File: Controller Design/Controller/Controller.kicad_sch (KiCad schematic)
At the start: 48 parts, among them J1 USB_C_Receptacle_USB2.0, J2 JTAG, J3 UART, J4 FAN0, J5 FAN1, J6 FAN2, SW1 SW_MEC_5G, SW2 BOOT, SW3 RotaryEncoder_Switch, U1 ESP32-S3-WROOM-2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

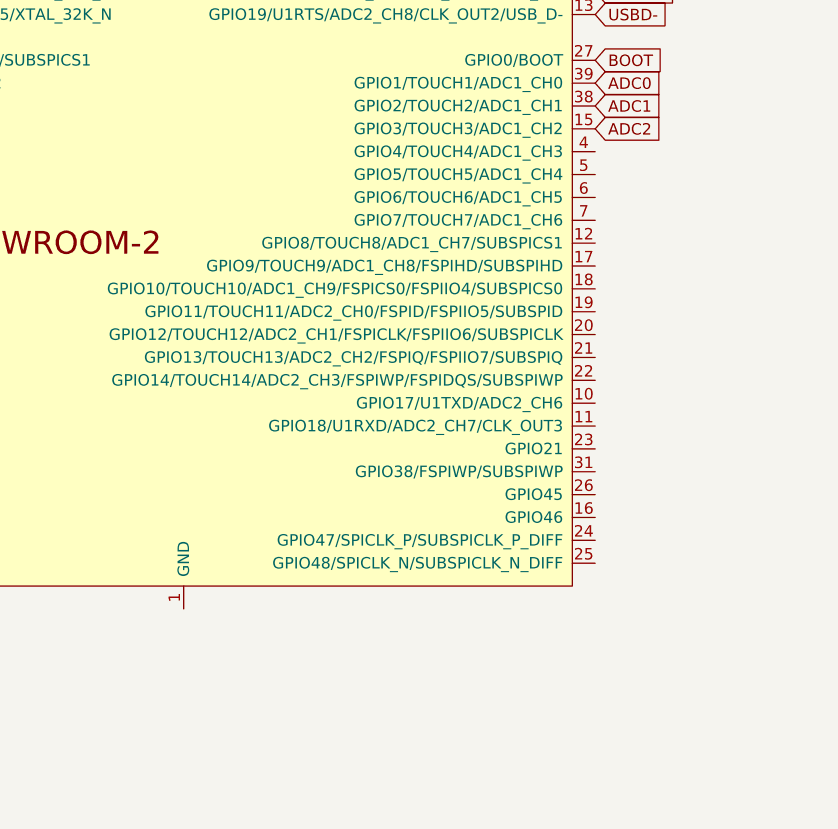
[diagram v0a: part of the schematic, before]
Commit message: devlog: concerns with power
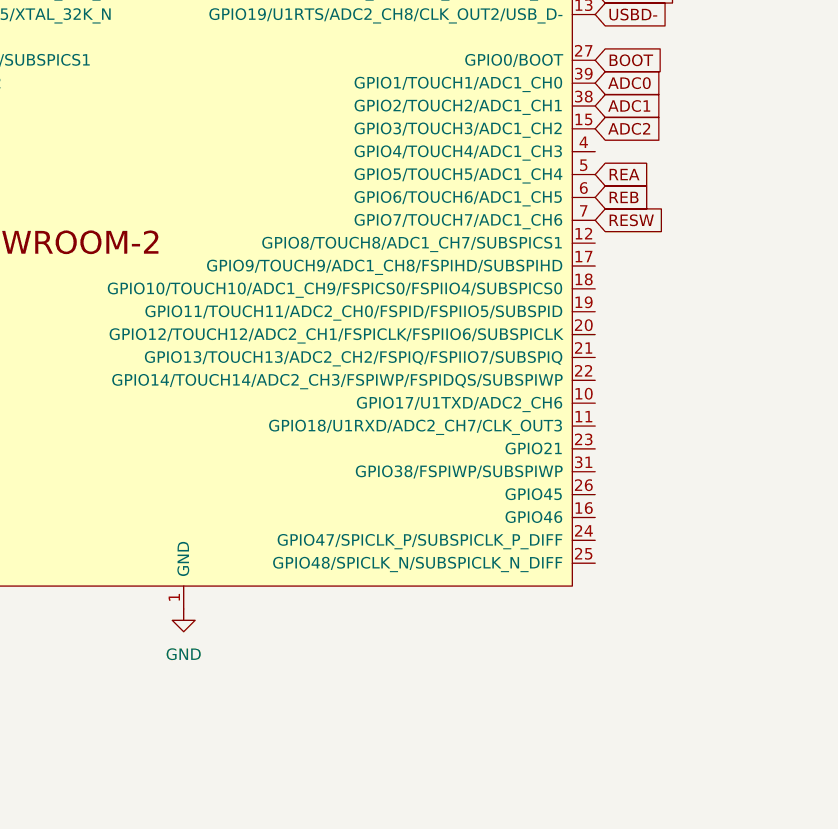
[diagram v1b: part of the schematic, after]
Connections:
- net GND: now also U1.1 (GND), U1.40 (GND), U1.41 (GND)
- net REA: now also U1.5 (GPIO5/TOUCH5/ADC1_CH4)
- net REB: now also U1.6 (GPIO6/TOUCH6/ADC1_CH5)
- net RESW: now also U1.7 (GPIO7/TOUCH7/ADC1_CH6)
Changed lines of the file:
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@@
+    )
+  )
+  (global_label "RESW" (shape input) (at 144.78 102.87 0) (fields_autoplaced)
+    (effects (font (size 1.27 1.27)) (justify left))
+    (property "Intersheetrefs" "${INTERSHEET_REFS}" (at 154.0357 102.87 0)
+      (effects (font (size 1.27 1.27)) (justify left) hide)
     )
   )
@@
     )
   )
+  (global_label "REB" (shape input) (at 144.78 100.33 0) (fields_autoplaced)
+    (effects (font (size 1.27 1.27)) (justify left))
+    (property "Intersheetrefs" "${INTERSHEET_REFS}" (at 151.3748 100.33 0)
+      (effects (font (size 1.27 1.27)) (justify left) hide)
+    )
+  )
   (global_label "TMS" (shape input) (at 229.87 114.3 180) (fields_autoplaced)
     (effects (font (size 1.27 1.27)) (justify right))
@@
     (effects (font (size 1.27 1.27)) (justify left))
     (property "Intersheetrefs" "${INTERSHEET_REFS}" (at 154.3382 80.01 0)
+      (effects (font (size 1.27 1.27)) (justify left) hide)
+    )
+  )
+  (global_label "REA" (shape input) (at 144.78 97.79 0) (fields_autoplaced)
+    (effects (font (size 1.27 1.27)) (justify left))
+    (property "Intersheetrefs" "${INTERSHEET_REFS}" (at 151.1934 97.79 0)
       (effects (font (size 1.27 1.27)) (justify left) hide)
     )
@@
         )
       )
+    )
+  )
+  (symbol (lib_id "power:GND") (at 99.06 146.05 0) (unit 1)
+    (in_bom yes) (on_board yes) (dnp no) (fields_autoplaced)
+    (property "Reference" "#PWR038" (at 99.06 152.4 0)
+      (effects (font (size 1.27 1.27)) hide)
+    )
+    (property "Value" "GND" (at 99.06 151.13 0)
+      (effects (font (size 1.27 1.27)))
+    )
+    (property "Footprint" "" (at 99.06 146.05 0)
+      (effects (font (size 1.27 1.27)) hide)
+    )
+    (property "Datasheet" "" (at 99.06 146.05 0)
+      (effects (font (size 1.27 1.27)) hide)
+    )
+    (pin "1")
+    (instances
+      (project "Controller"
+        (path "/3ce940e4-bb4c-4a70-948a-7cd3ff5c738d"
+          (reference "#PWR038") (unit 1)
+        )
+      )

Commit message: cleaned up schematic
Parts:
- added D1, D2: D_Schottky, Diode_SMD:D_0805_2012Metric_Pad1.15x1.40mm_HandSolder, symbol Device:D_Schottky
- added J7: Molex Socket, symbol Connector:Conn_01x04_Socket
- added U5: AP2112K-3.3, Package_TO_SOT_SMD:SOT-23-5, symbol Regulator_Linear:AP2112K-3.3
- C1, C10, C11, C2, C3, C4, C5, C6, C7, C8, C9: footprint (none) -> Capacitor_SMD:C_0805_2012Metric_Pad1.18x1.45mm_HandSolder
- R1, R11, R12, R15, R16, R18, R2, R3, R4, R5, R6, R7, R8, R9, TH1: footprint (none) -> Resistor_SMD:R_0805_2012Metric_Pad1.20x1.40mm_HandSolder
- R10, R13, R14, R17: value 60k -> 50k; footprint (none) -> Resistor_SMD:R_0805_2012Metric_Pad1.20x1.40mm_HandSolder
- R19, R20, R21: value R -> 1k; footprint (none) -> Resistor_SMD:R_0805_2012Metric_Pad1.20x1.40mm_HandSolder
- SW1: value SW_MEC_5G -> RESET
- U2, U3, U4: value Opamp_Dual -> LM2904DR; footprint (none) -> Package_SO:SOIC-8_3.9x4.9mm_P1.27mm
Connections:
- net +3.3V: now also U5.5 (VOUT)
- net GND: now also J7.2 (Pin_2), J7.3 (Pin_3), U5.2 (GND)
- net 5vUsb: now reaches J1.A4 (VBUS), J1.A9 (VBUS), J1.B4 (VBUS), J1.B9 (VBUS)
- net 5vUsb: now also D1.2 (A)
- new net: D1.1 (K), D2.1 (K), U5.1 (VIN), U5.3 (EN)
- new net 5vMol: D2.2 (A), J7.4 (Pin_4)
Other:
- moved on the sheet: C1, C10, C11, C2, C3, C4, C5, C6, C7, C8, C9, J1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
